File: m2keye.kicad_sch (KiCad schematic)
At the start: 17 parts

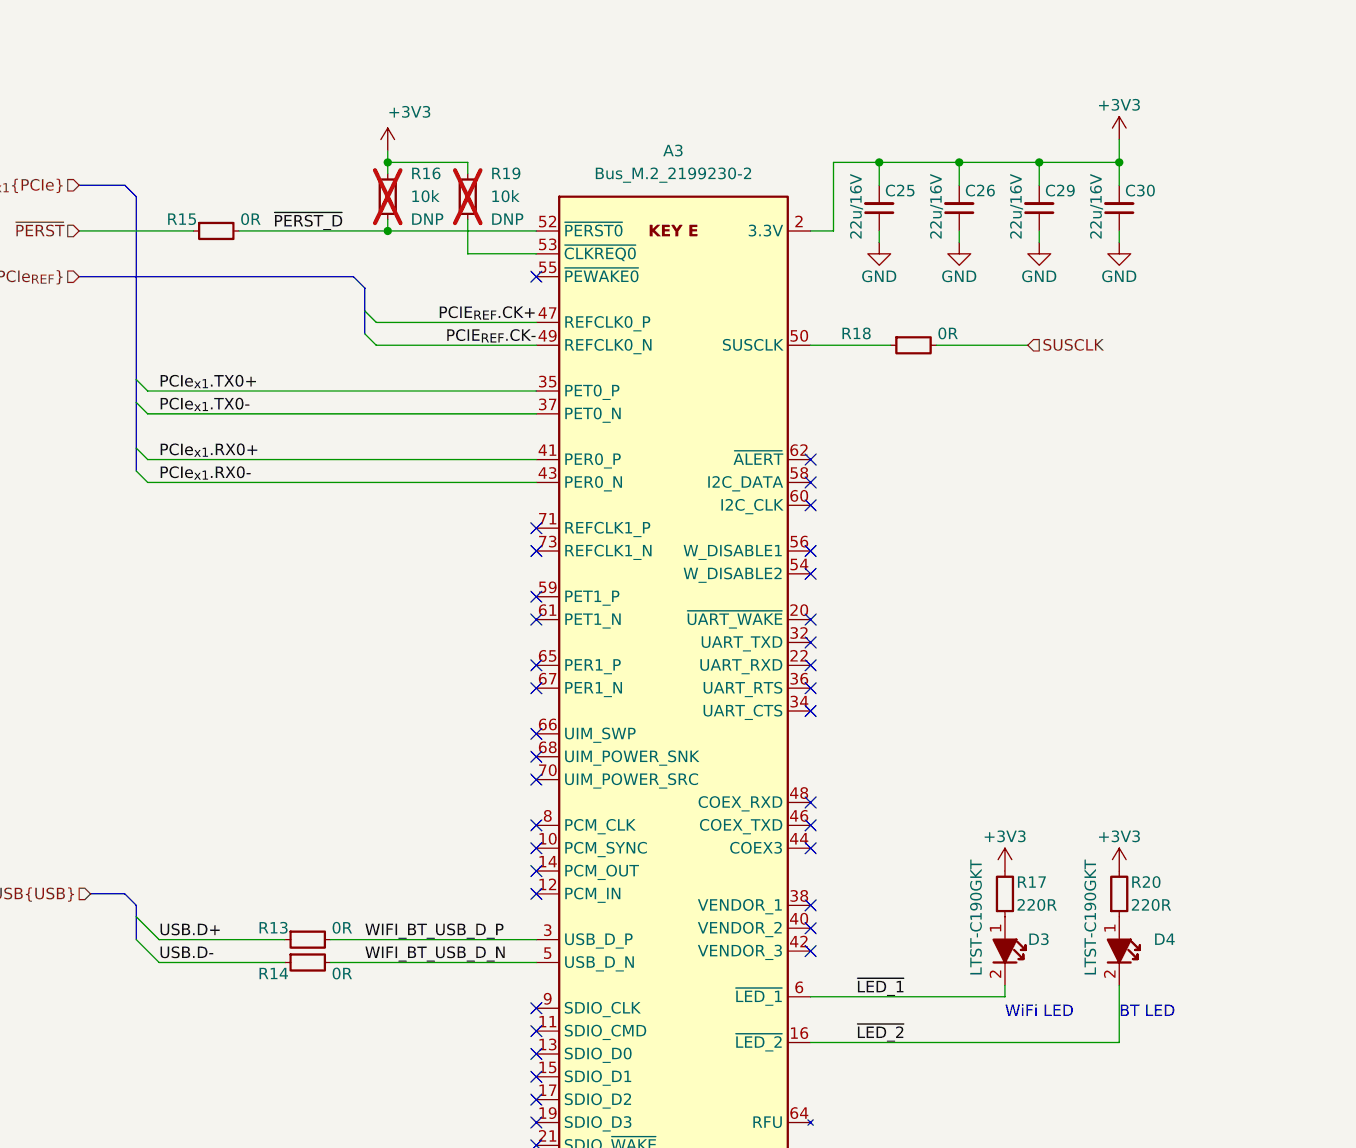
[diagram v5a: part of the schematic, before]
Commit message: [#58137] Update backplane connector pinout
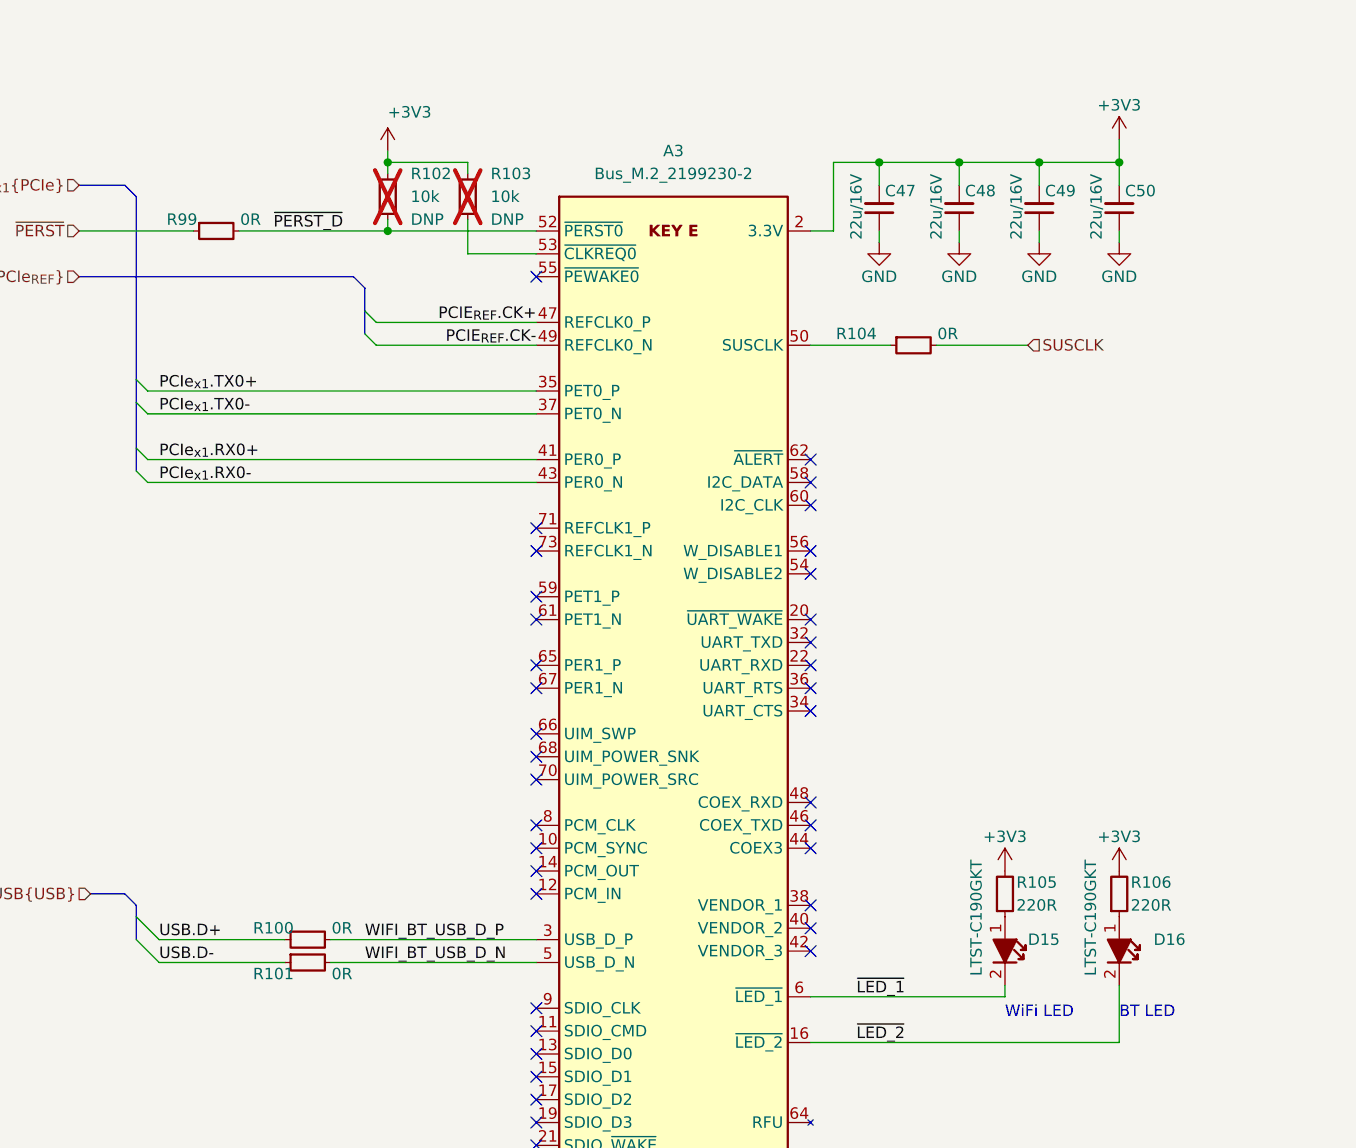
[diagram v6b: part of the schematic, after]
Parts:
- renumbered C25 to C47, C26 to C48, C29 to C49, C30 to C50, D3 to D15, D4 to D16, R13 to R100, R14 to R101, R16 to R102, R19 to R103, R18 to R104, R17 to R105, R20 to R106, R15 to R99

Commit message: Fix ERC
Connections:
- no-connect marks 38 -> 42
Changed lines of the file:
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@@
   (no_connect (at 213.36 128.27))
   (no_connect (at 182.88 181.61))
+  (no_connect (at 157.48 118.11))
   (no_connect (at 182.88 151.13))
   (no_connect (at 182.88 125.73))
@@
   (no_connect (at 213.36 162.56))
   (no_connect (at 182.88 173.99))
+  (no_connect (at 157.48 125.73))
   (no_connect (at 182.88 138.43))
   (no_connect (at 213.36 120.65))
   (no_connect (at 213.36 135.89))
+  (no_connect (at 157.48 120.65))
   (no_connect (at 182.88 179.07))
   (no_connect (at 182.88 123.19))
@@
   (no_connect (at 213.36 125.73))
   (no_connect (at 213.36 151.13))
+  (no_connect (at 157.48 128.27))
+  (bus_entry (at 139.7 118.11) (size -1.27 -1.27)
+    (stroke (width 0) (type default))
+  )
   (bus_entry (at 138.43 161.29) (size 2.54 2.54)
     (stroke (width 0) (type default))
@@
     (stroke (width 0) (type default))
   )
+  (bus_entry (at 139.7 128.27) (size -1.27 -1.27)
+    (stroke (width 0) (type default))
+  )
   (bus_entry (at 165.1 92.71) (size -1.27 -1.27)
     (stroke (width 0) (type default))
@@
     (stroke (width 0) (type default))
   )
+  (bus_entry (at 139.7 120.65) (size -1.27 -1.27)
+    (stroke (width 0) (type default))
+  )
+  (bus_entry (at 139.7 125.73) (size -1.27 -1.27)
+    (stroke (width 0) (type default))
+  )
   (wire (pts (xy 139.7 100.33) (xy 182.88 100.33))
     (stroke (width 0) (type default))
@@
     (stroke (width 0) (type default))
   )
+  (wire (pts (xy 157.48 118.11) (xy 139.7 118.11))
+    (stroke (width 0) (type default))
+  )
   (wire (pts (xy 218.44 189.23) (xy 218.44 190.5))
     (stroke (width 0) (type default))
@@
     (stroke (width 0) (type default))
   )
+  (bus (pts (xy 138.43 116.84) (xy 138.43 119.38))
+    (stroke (width 0) (type default))
+  )
+  (wire (pts (xy 157.48 128.27) (xy 139.7 128.27))
+    (stroke (width 0) (type default))
+  )
   (wire (pts (xy 220.98 74.93) (xy 220.98 77.47))
     (stroke (width 0) (type default))
@@
     (stroke (width 0) (type default))
   )
+  (bus (pts (xy 138.43 124.46) (xy 138.43 127))
+    (stroke (width 0) (type default))
+  )
   (wire (pts (xy 175.26 74.93) (xy 175.26 76.2))
     (stroke (width 0) (type default))
   )
+  (wire (pts (xy 157.48 125.73) (xy 139.7 125.73))
+    (stroke (width 0) (type default))
+  )
   (wire (pts (xy 182.88 92.71) (xy 165.1 92.71))
     (stroke (width 0) (type default))
@@
     (stroke (width 0) (type default))
   )
+  (wire (pts (xy 157.48 120.65) (xy 139.7 120.65))
+    (stroke (width 0) (type default))
+  )
   (wire (pts (xy 238.76 74.93) (xy 247.65 74.93))
     (stroke (width 0) (type default))
@@
     (stroke (width 0) (type default))
   )
+  (bus (pts (xy 138.43 119.38) (xy 138.43 124.46))
+    (stroke (width 0) (type default))
+  )
   (wire (pts (xy 139.7 102.87) (xy 182.88 102.87))
     (stroke (width 0) (type default))
@@
   )
   (wire (pts (xy 140.97 161.29) (xy 154.94 161.29))
+    (stroke (width 0) (type default))
+  )
+  (bus (pts (xy 138.43 109.22) (xy 138.43 116.84))
     (stroke (width 0) (type default))
   )
@@
     (effects (font (size 1.27 1.27)) (justify left bottom))
   )
+  (label "PCIe_{x1}.RX1+" (at 157.48 125.73 180) (fields_autoplaced)
+    (effects (font (size 1.27 1.27)) (justify right bottom))
+  )
   (label "WIFI_BT_USB_D_P" (at 163.83 161.29 0) (fields_autoplaced)
     (effects (font (size 1.27 1.27)) (justify left bottom))
@@
     (effects (font (size 1.27 1.27)) (justify left bottom))
   )
+  (label "PCIe_{x1}.RX1-" (at 157.48 128.27 180) (fields_autoplaced)
+    (effects (font (size 1.27 1.27)) (justify right bottom))
+  )
   (label "PCIE_{REF}.CK-" (at 182.88 95.25 180) (fields_autoplaced)
     (effects (font (size 1.27 1.27)) (justify right bottom))
@@
     (effects (font (size 1.27 1.27)) (justify left bottom))
   )
+  (label "PCIe_{x1}.TX1-" (at 157.48 120.65 180) (fields_autoplaced)
+    (effects (font (size 1.27 1.27)) (justify right bottom))
+  )
+  (label "PCIe_{x1}.TX1+" (at 157.48 118.11 180) (fields_autoplaced)
+    (effects (font (size 1.27 1.27)) (justify right bottom))
+  )
   (label "~{PERST_D}" (at 153.67 82.55 0) (fields_autoplaced)

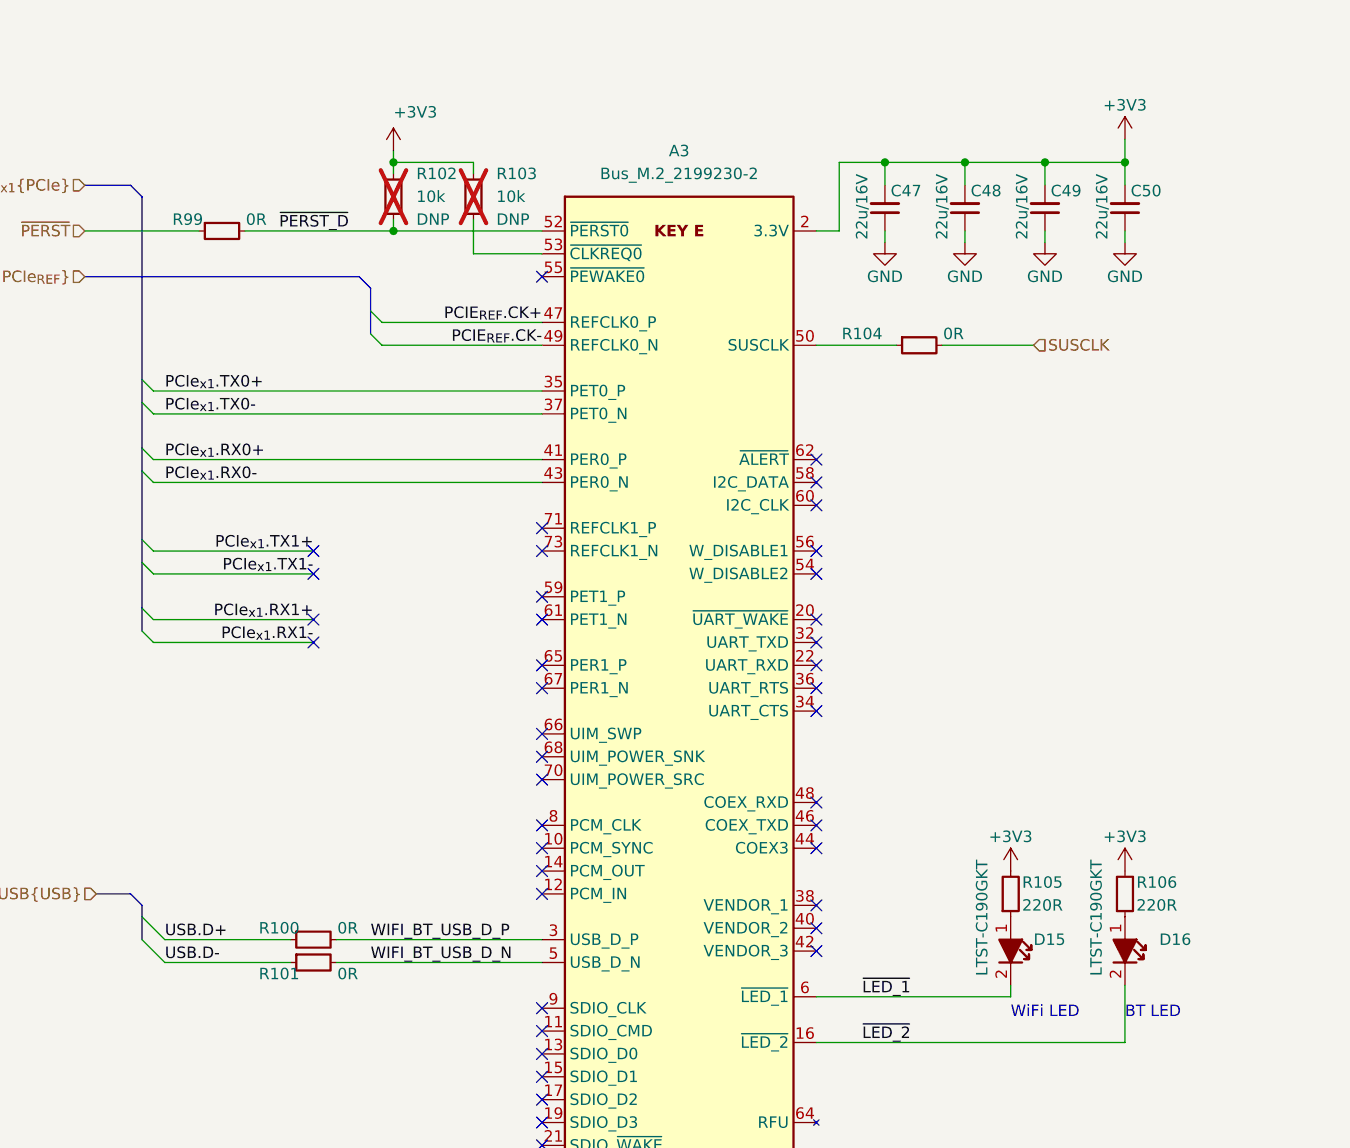
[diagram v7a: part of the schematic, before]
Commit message: Reannotate schematic
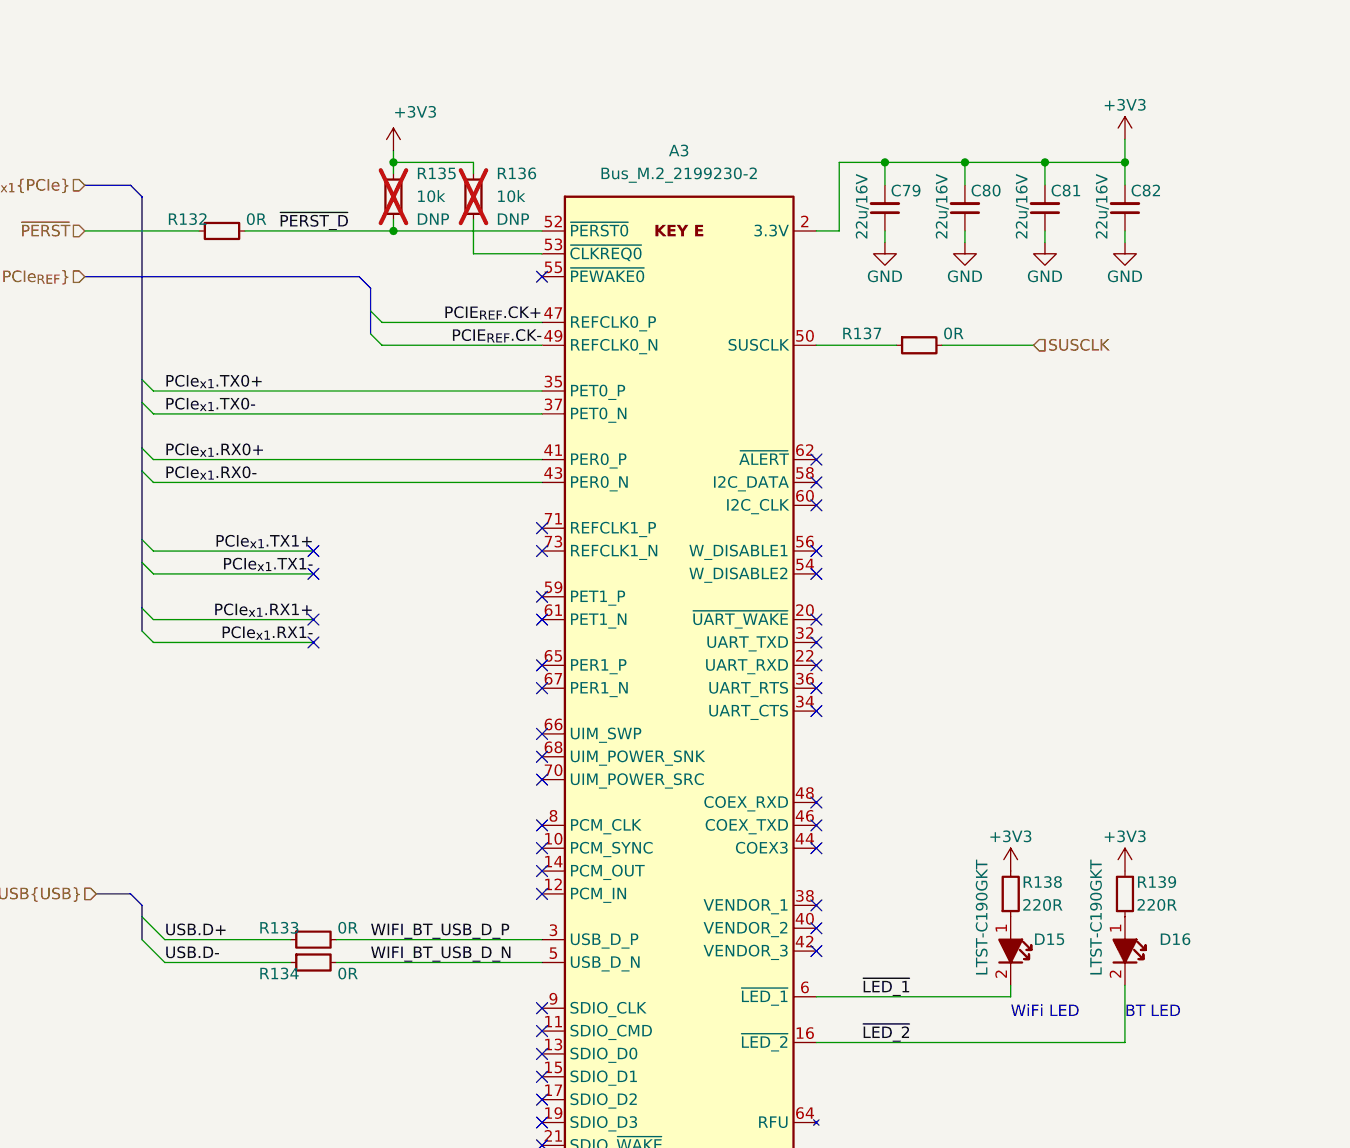
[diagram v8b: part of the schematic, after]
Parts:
- renumbered C47 to C79, C48 to C80, C49 to C81, C50 to C82, R99 to R132, R100 to R133, R101 to R134, R102 to R135, R103 to R136, R104 to R137, R105 to R138, R106 to R139
